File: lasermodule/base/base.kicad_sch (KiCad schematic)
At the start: 18 parts, among them J10 Conn_01x01, J11 Conn_01x01, J12 Conn_01x01, J19 2-1734248-0, J2 Conn_01x13, J6 mirrormotor, J7 Conn_01x01, J8 Conn_01x01, J9 Conn_01x01

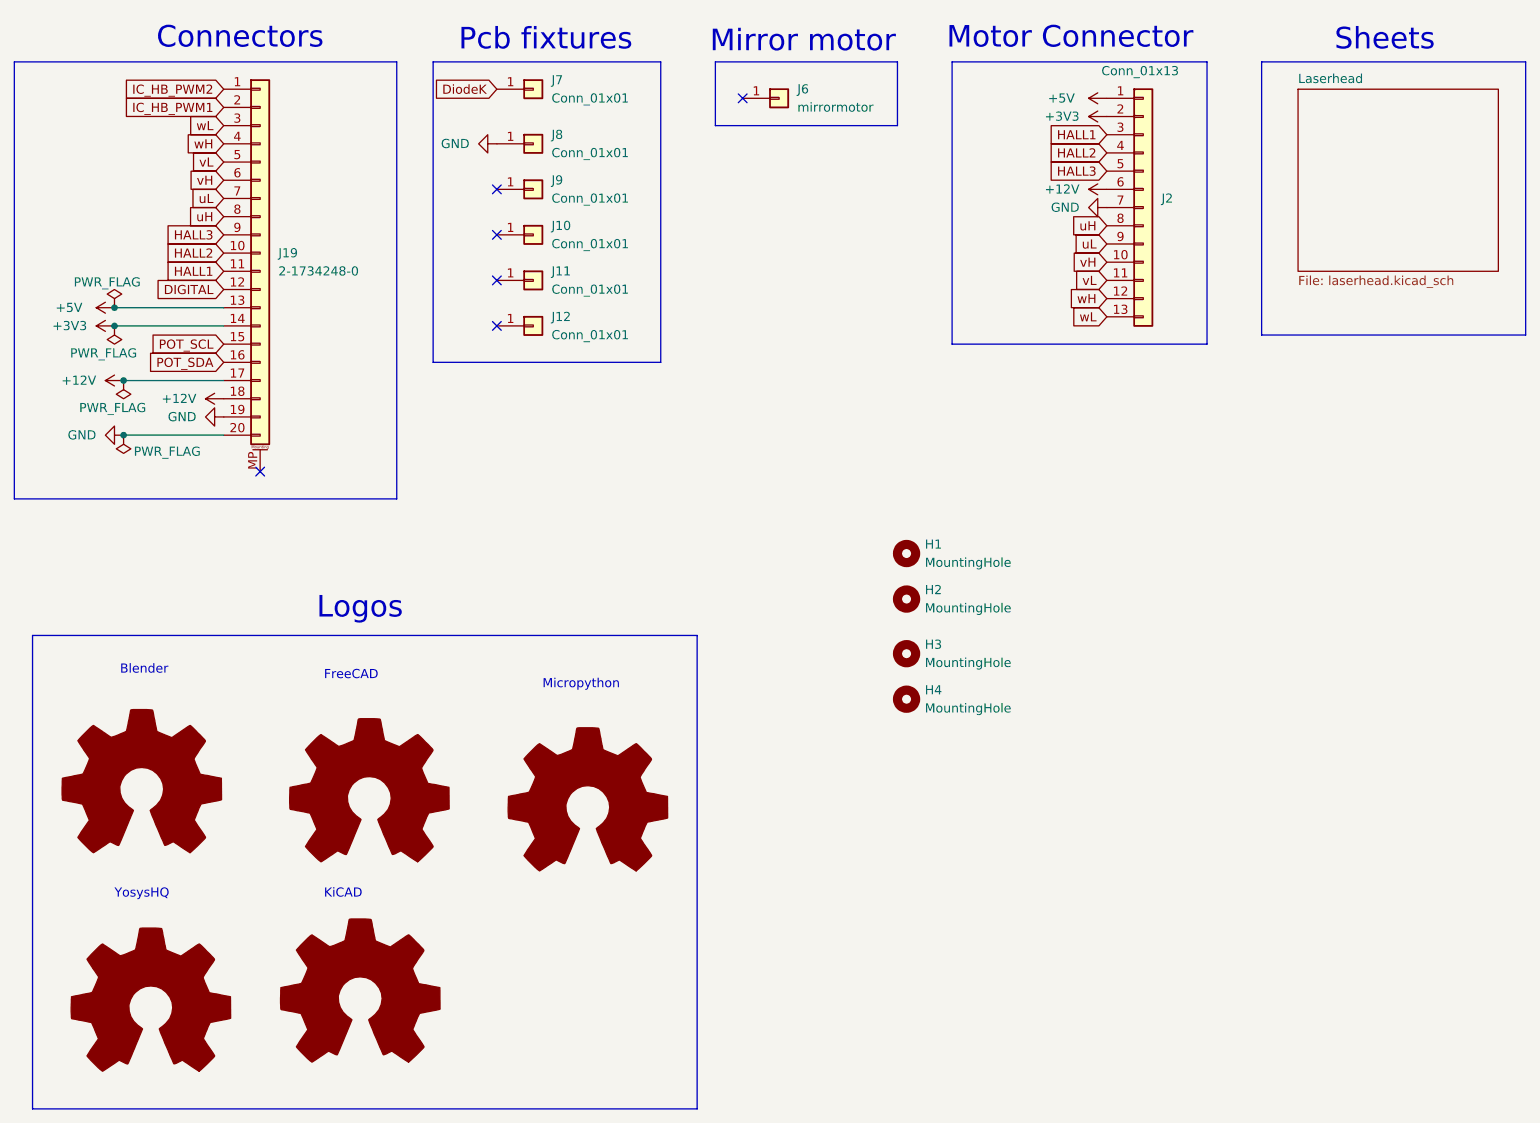
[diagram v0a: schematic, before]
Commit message: added mount felixprinter, standoffs
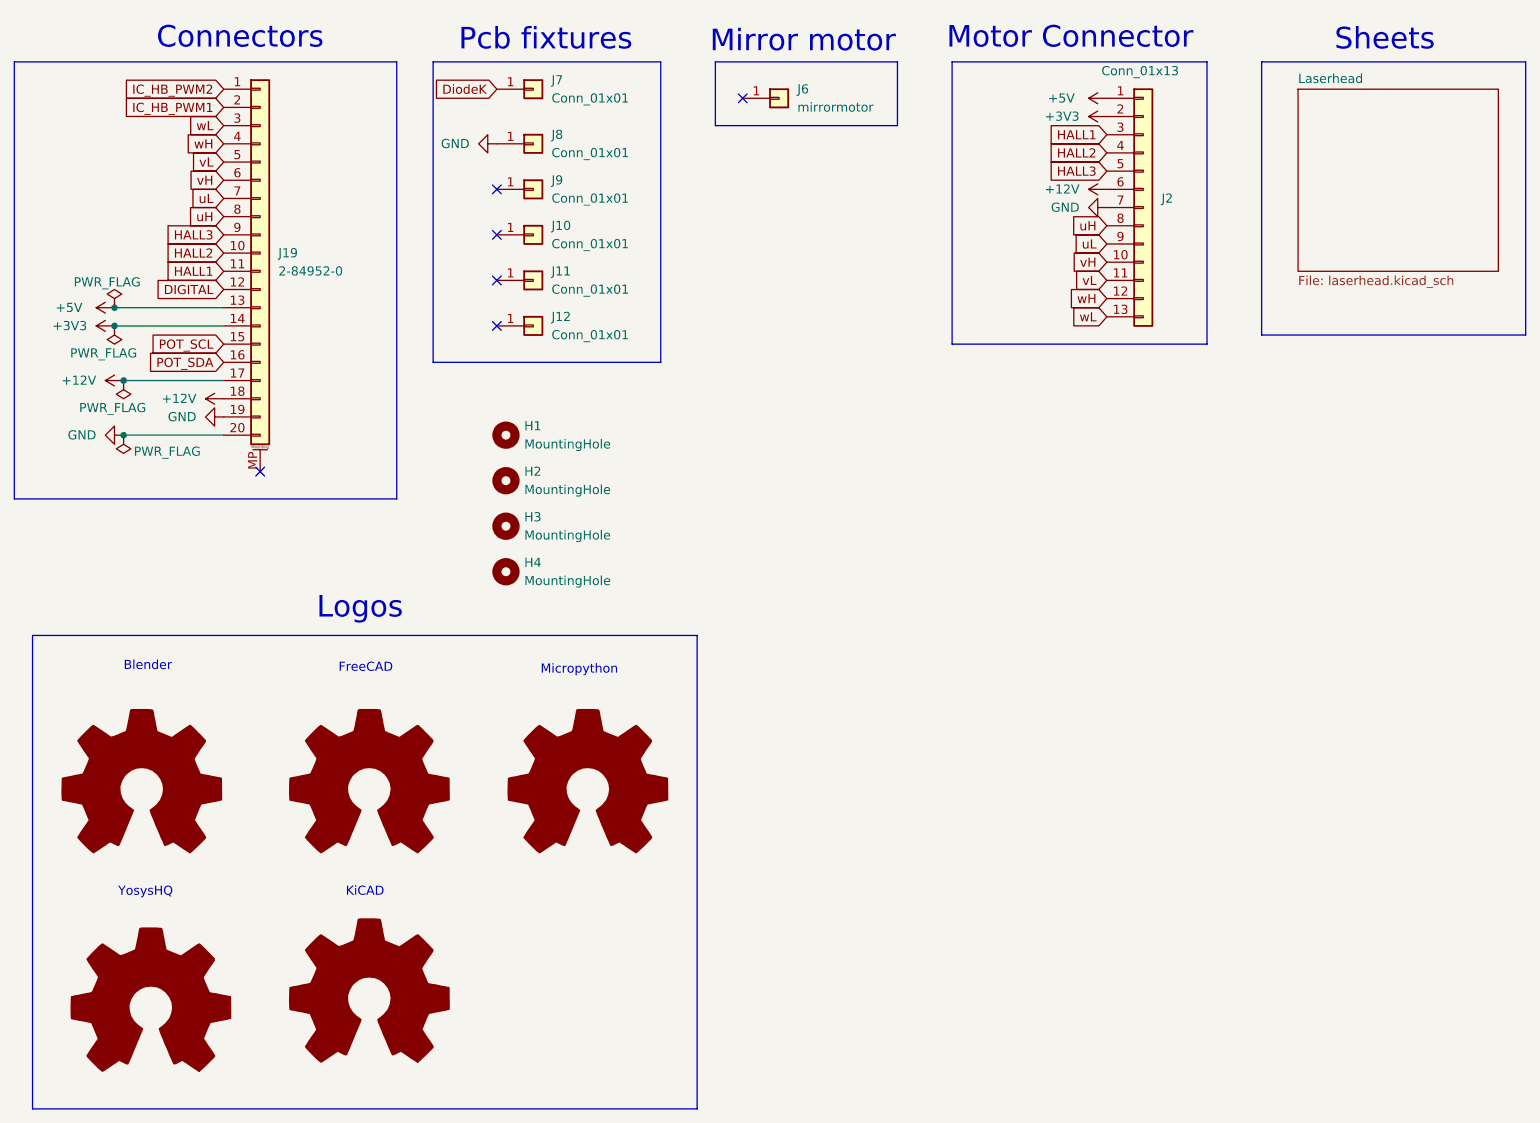
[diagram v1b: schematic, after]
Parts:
- H1, H2, H3, H4: manf# (none) -> 970050244; mouser# (none) -> 710-970050244
- J19: value 2-1734248-0 -> 2-84952-0
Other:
- moved on the sheet: H1, H2, H3, H4
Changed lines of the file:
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@@
 	(text "Micropython"
 		(exclude_from_sim no)
-		(at 101.6 129.54 0)
+		(at 101.346 127.508 0)
 		(effects
 			(font
@@
 	(text "YosysHQ"
 		(exclude_from_sim no)
-		(at 41.91 158.75 0)
+		(at 42.418 158.496 0)
 		(effects
 			(font
@@
 	(text "FreeCAD"
 		(exclude_from_sim no)
-		(at 71.12 128.27 0)
+		(at 73.152 127.254 0)
 		(effects
 			(font
@@
 	(text "KiCAD"
 		(exclude_from_sim no)
-		(at 71.12 158.75 0)
+		(at 74.168 158.496 0)
 		(effects
 			(font
@@
 	(text "Blender"
 		(exclude_from_sim no)
-		(at 42.672 127.508 0)
+		(at 43.18 127 0)
 		(effects
 			(font
@@
 	(symbol
 		(lib_id "Graphic:Logo_Open_Hardware_Large")
-		(at 76.2 172.72 0)
+		(at 77.47 172.72 0)
 		(unit 1)
 		(exclude_from_sim no)
@@
 		(dnp no)
 		(property "Reference" "L3"
-			(at 76.2 160.02 0)
+			(at 77.47 160.02 0)
 			(effects
 				(font
@@
 		)
 		(property "Value" "Logo_Open_Hardware_Large"
-			(at 76.2 182.88 0)
+			(at 77.47 182.88 0)
 			(effects
 				(font
@@
 		)
 		(property "Footprint" "sockets_scanhead:kicad"
-			(at 76.2 172.72 0)
+			(at 77.47 172.72 0)
 			(effects
 				(font
@@
 		)
 		(property "Datasheet" "~"
-			(at 76.2 172.72 0)
+			(at 77.47 172.72 0)
 			(effects
 				(font
@@
 		)
 		(property "Description" ""
-			(at 76.2 172.72 0)
+			(at 77.47 172.72 0)
 			(effects
 				(font
@@
 	(symbol
 		(lib_id "Mechanical:MountingHole")
-		(at 152.4 130.81 0)
+		(at 96.52 113.03 0)
 		(unit 1)
 		(exclude_from_sim yes)
@@
 		(fields_autoplaced yes)
 		(property "Reference" "H4"
-			(at 154.94 129.5399 0)
+			(at 99.06 111.7599 0)
 			(effects
 				(font
@@
 		)
 		(property "Value" "MountingHole"
-			(at 154.94 132.0799 0)
+			(at 99.06 114.2999 0)
 			(effects
 				(font
@@
 		)
 		(property "Footprint" "MountingHole:MountingHole_2.2mm_M2"
-			(at 152.4 130.81 0)
+			(at 96.52 113.03 0)
 			(effects
 				(font
@@
 		)
 		(property "Datasheet" "~"
-			(at 152.4 130.81 0)
+			(at 96.52 113.03 0)
 			(effects
 				(font
@@
 		)
 		(property "Description" "Mounting Hole without connection"
-			(at 152.4 130.81 0)
+			(at 96.52 113.03 0)
+			(effects
+				(font
+					(size 1.27 1.27)
+				)
+				(hide yes)
+			)
+		)
+		(property "manf#" "970050244"
+			(at 96.52 113.03 0)
+			(effects
+				(font
+					(size 1.27 1.27)
+				)
+				(hide yes)
+			)
+		)
+		(property "mouser#" "710-970050244"
+			(at 96.52 113.03 0)
 			(effects
 				(font
@@
 			)
 		)
-		(property "Value" "2-1734248-0"
+		(property "Value" "2-84952-0"
 			(at 64.77 71.1199 0)
 			(effects
@@
 	(symbol
 		(lib_id "Graphic:Logo_Open_Hardware_Large")
-		(at 107.95 146.05 0)
+		(at 107.95 143.51 0)
 		(unit 1)
 		(exclude_from_sim no)
@@
 		(dnp no)
 		(property "Reference" "L5"
-			(at 107.95 133.35 0)
+			(at 107.95 130.81 0)
 			(effects
 				(font
@@
 		)
 		(property "Value" "Logo_Open_Hardware_Large"
-			(at 107.95 156.21 0)
+			(at 107.95 153.67 0)
 			(effects
 				(font
@@
 		)
 		(property "Footprint" "sockets_scanhead:micropython"
-			(at 107.95 146.05 0)
+			(at 107.95 143.51 0)
 			(effects
 				(font
@@
 		)
 		(property "Datasheet" "~"
-			(at 107.95 146.05 0)
+			(at 107.95 143.51 0)
 			(effects
 				(font
@@
 		)
 		(property "Description" ""
-			(at 107.95 146.05 0)
+			(at 107.95 143.51 0)
 			(effects
 				(font
@@
 	(symbol
 		(lib_id "Mechanical:MountingHole")
-		(at 152.4 124.46 0)
+		(at 96.52 106.68 0)
 		(unit 1)
 		(exclude_from_sim yes)
@@
 		(fields_autoplaced yes)
 		(property "Reference" "H3"
-			(at 154.94 123.1899 0)
+			(at 99.06 105.4099 0)
 			(effects
 				(font
@@
 		)
 		(property "Value" "MountingHole"
-			(at 154.94 125.7299 0)
+			(at 99.06 107.9499 0)
 			(effects
 				(font
@@
 		)
 		(property "Footprint" "MountingHole:MountingHole_2.2mm_M2"
-			(at 152.4 124.46 0)
+			(at 96.52 106.68 0)
 			(effects
 				(font
@@
 		)
 		(property "Datasheet" "~"
-			(at 152.4 124.46 0)
+			(at 96.52 106.68 0)
 			(effects
 				(font
@@
 		)
 		(property "Description" "Mounting Hole without connection"
-			(at 152.4 124.46 0)
+			(at 96.52 106.68 0)
+			(effects
+				(font
+					(size 1.27 1.27)
+				)
+				(hide yes)
+			)
+		)
+		(property "manf#" "970050244"
+			(at 96.52 106.68 0)
+			(effects
+				(font
+					(size 1.27 1.27)
+				)
+				(hide yes)
+			)
+		)
+		(property "mouser#" "710-970050244"
+			(at 96.52 106.68 0)
 			(effects
 				(font
@@
 	(symbol
 		(lib_id "Mechanical:MountingHole")
-		(at 152.4 110.49 0)
+		(at 96.52 93.98 0)
 		(unit 1)
 		(exclude_from_sim yes)
@@
 		(fields_autoplaced yes)
 		(property "Reference" "H1"
-			(at 154.94 109.2199 0)
+			(at 99.06 92.7099 0)
 			(effects
 				(font
@@
 		)
 		(property "Value" "MountingHole"
-			(at 154.94 111.7599 0)
+			(at 99.06 95.2499 0)
 			(effects
 				(font
@@
 		)
 		(property "Footprint" "MountingHole:MountingHole_2.2mm_M2"
-			(at 152.4 110.49 0)
+			(at 96.52 93.98 0)
 			(effects
 				(font
@@
 		)
 		(property "Datasheet" "~"
-			(at 152.4 110.49 0)
+			(at 96.52 93.98 0)
 			(effects
 				(font
@@
 		)
 		(property "Description" "Mounting Hole without connection"
-			(at 152.4 110.49 0)
+			(at 96.52 93.98 0)
+			(effects
+				(font
+					(size 1.27 1.27)
+				)
+				(hide yes)
+			)
+		)
+		(property "mouser#" "710-970050244"
+			(at 96.52 93.98 0)
+			(effects
+				(font
+					(size 1.27 1.27)
+				)
+				(hide yes)
+			)
+		)
+		(property "manf#" "970050244"
+			(at 96.52 93.98 0)
 			(effects
 				(font
@@
 	(symbol
 		(lib_id "Mechanical:MountingHole")
-		(at 152.4 116.84 0)
+		(at 96.52 100.33 0)
 		(unit 1)
 		(exclude_from_sim yes)
@@
 		(fields_autoplaced yes)
 		(property "Reference" "H2"
-			(at 154.94 115.5699 0)
+			(at 99.06 99.0599 0)
 			(effects
 				(font
@@
 		)
 		(property "Value" "MountingHole"
-			(at 154.94 118.1099 0)
+			(at 99.06 101.5999 0)
 			(effects
 				(font
@@
 		)
 		(property "Footprint" "MountingHole:MountingHole_2.2mm_M2"
-			(at 152.4 116.84 0)
+			(at 96.52 100.33 0)
 			(effects
 				(font
@@
 		)
 		(property "Datasheet" "~"
-			(at 152.4 116.84 0)
+			(at 96.52 100.33 0)
 			(effects
 				(font
@@
 		)
 		(property "Description" "Mounting Hole without connection"
-			(at 152.4 116.84 0)
+			(at 96.52 100.33 0)
+			(effects
+				(font
+					(size 1.27 1.27)
+				)
+				(hide yes)
+			)
+		)
+		(property "manf#" "970050244"
+			(at 96.52 100.33 0)
+			(effects
+				(font
+					(size 1.27 1.27)
+				)
+				(hide yes)
+			)
+		)
+		(property "mouser#" "710-970050244"
+			(at 96.52 100.33 0)
 			(effects
 				(font
@@
 	(symbol
 		(lib_id "Graphic:Logo_Open_Hardware_Large")
-		(at 77.47 144.78 0)
+		(at 77.47 143.51 0)
 		(unit 1)
 		(exclude_from_sim no)
@@
 		(dnp no)
 		(property "Reference" "L4"
-			(at 77.47 132.08 0)
+			(at 77.47 130.81 0)
 			(effects
 				(font
@@
 		)
 		(property "Value" "Logo_Open_Hardware_Large"
-			(at 77.47 154.94 0)
+			(at 77.47 153.67 0)
 			(effects
 				(font
@@
 		)
 		(property "Footprint" "sockets_scanhead:freecad"
-			(at 77.47 144.78 0)
+			(at 77.47 143.51 0)
 			(effects
 				(font
@@
 		)
 		(property "Datasheet" "~"
-			(at 77.47 144.78 0)
+			(at 77.47 143.51 0)
 			(effects
 				(font
@@
 		)
 		(property "Description" ""
-			(at 77.47 144.78 0)
-			(effects
-				(font
+			(at 77.47 143.51 0)
+			(effects
+				(font

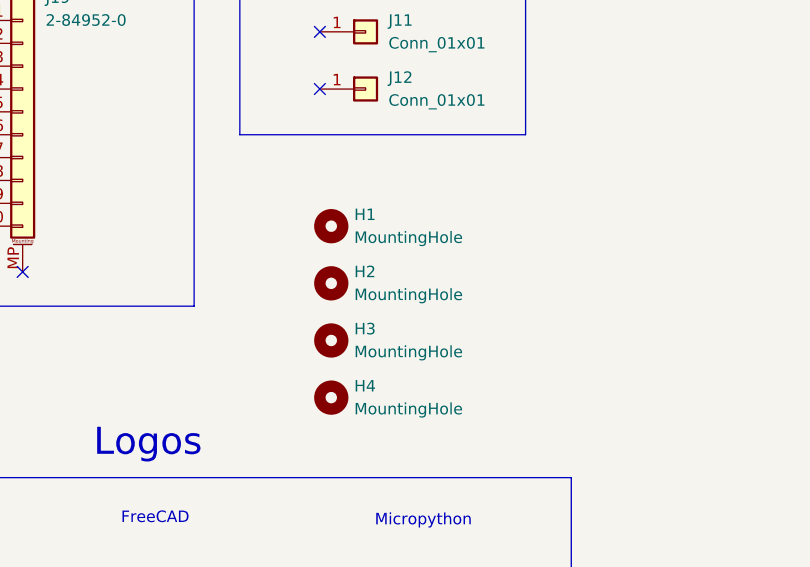
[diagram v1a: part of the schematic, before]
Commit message: changes to reduce prices pcbway
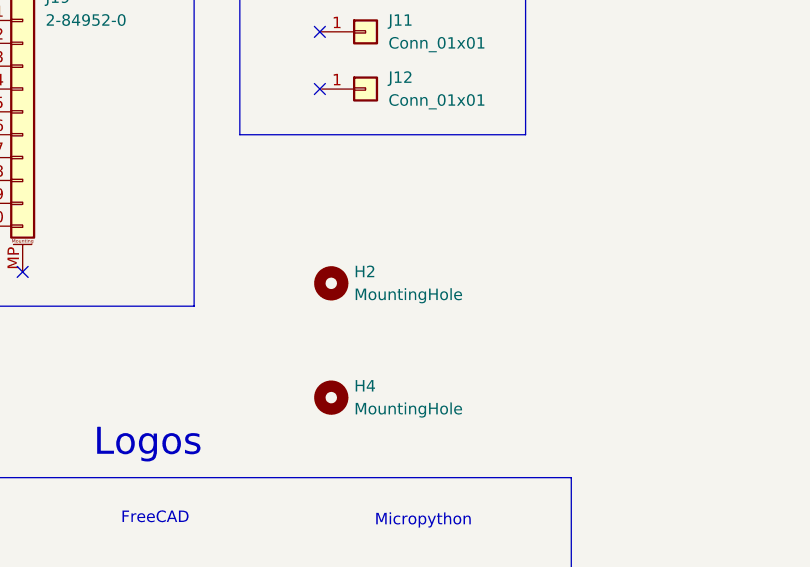
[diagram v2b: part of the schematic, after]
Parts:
- removed H1, H3: MountingHole, MountingHole:MountingHole_2.2mm_M2, symbol Mechanical:MountingHole
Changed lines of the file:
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@@
-	)
-	(symbol
-		(lib_id "Mechanical:MountingHole")
-		(at 96.52 106.68 0)
-		(unit 1)
-		(exclude_from_sim yes)
-		(in_bom no)
-		(on_board yes)
-		(dnp no)
-		(fields_autoplaced yes)
-		(property "Reference" "H3"
-			(at 99.06 105.4099 0)
-			(effects
-				(font
-					(size 1.27 1.27)
-				)
-				(justify left)
-			)
-		)
-		(property "Value" "MountingHole"
-			(at 99.06 107.9499 0)
-			(effects
-				(font
-					(size 1.27 1.27)
-				)
-				(justify left)
-			)
-		)
-		(property "Footprint" "MountingHole:MountingHole_2.2mm_M2"
-			(at 96.52 106.68 0)
-			(effects
-				(font
-					(size 1.27 1.27)
-				)
-				(hide yes)
-			)
-		)
-		(property "Datasheet" "~"
-			(at 96.52 106.68 0)
-			(effects
-				(font
-					(size 1.27 1.27)
-				)
-				(hide yes)
-			)
-		)
-		(property "Description" "Mounting Hole without connection"
-			(at 96.52 106.68 0)
-			(effects
-				(font
-					(size 1.27 1.27)
-				)
-				(hide yes)
-			)
-		)
-		(property "manf#" "970050244"
-			(at 96.52 106.68 0)
-			(effects
-				(font
-					(size 1.27 1.27)
-				)
-				(hide yes)
-			)
-		)
-		(property "mouser#" "710-970050244"
-			(at 96.52 106.68 0)
-			(effects
-				(font
-					(size 1.27 1.27)
-				)
-				(hide yes)
-			)
-		)
-		(instances
-			(project "base"
-				(path "/e63e39d7-6ac0-4ffd-8aa3-1841a4541b55"
-					(reference "H3")
-					(unit 1)
-				)
-			)
-		)
 	)
 	(symbol
@@
 					(unit 1)
 				)
-			)
-		)
-	)
-	(symbol
-		(lib_id "Mechanical:MountingHole")
-		(at 96.52 93.98 0)
-		(unit 1)
-		(exclude_from_sim yes)
-		(in_bom no)
-		(on_board yes)
-		(dnp no)
-		(fields_autoplaced yes)
-		(property "Reference" "H1"
-			(at 99.06 92.7099 0)
-			(effects
-				(font
-					(size 1.27 1.27)
-				)
-				(justify left)
-			)
-		)
-		(property "Value" "MountingHole"
-			(at 99.06 95.2499 0)
-			(effects
-				(font
-					(size 1.27 1.27)
-				)
-				(justify left)
-			)
-		)
-		(property "Footprint" "MountingHole:MountingHole_2.2mm_M2"
-			(at 96.52 93.98 0)
-			(effects
-				(font
-					(size 1.27 1.27)
-				)
-				(hide yes)
-			)
-		)
-		(property "Datasheet" "~"
-			(at 96.52 93.98 0)
-			(effects
-				(font
-					(size 1.27 1.27)
-				)
-				(hide yes)
-			)
-		)
-		(property "Description" "Mounting Hole without connection"
-			(at 96.52 93.98 0)
-			(effects
-				(font
-					(size 1.27 1.27)
-				)
-				(hide yes)
-			)
-		)
-		(property "mouser#" "710-970050244"
-			(at 96.52 93.98 0)
-			(effects
-				(font
-					(size 1.27 1.27)
-				)
-				(hide yes)
-			)
-		)
-		(property "manf#" "970050244"
-			(at 96.52 93.98 0)
-			(effects
-				(font
-					(size 1.27 1.27)
-				)
-				(hide yes)
-			)
-		)
-		(instances
-			(project "base"
-				(path "/e63e39d7-6ac0-4ffd-8aa3-1841a4541b55"
-					(reference "H1")
-					(unit 1)
-				)

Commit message: sent to pcbway
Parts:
- added H1, H3: MountingHole, MountingHole:MountingHole_2.2mm_M2, symbol Mechanical:MountingHole
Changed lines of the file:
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@@
+	)
+	(symbol
+		(lib_id "Mechanical:MountingHole")
+		(at 96.52 93.98 0)
+		(unit 1)
+		(exclude_from_sim yes)
+		(in_bom no)
+		(on_board yes)
+		(dnp no)
+		(fields_autoplaced yes)
+		(property "Reference" "H1"
+			(at 99.06 92.7099 0)
+			(effects
+				(font
+					(size 1.27 1.27)
+				)
+				(justify left)
+			)
+		)
+		(property "Value" "MountingHole"
+			(at 99.06 95.2499 0)
+			(effects
+				(font
+					(size 1.27 1.27)
+				)
+				(justify left)
+			)
+		)
+		(property "Footprint" "MountingHole:MountingHole_2.2mm_M2"
+			(at 96.52 93.98 0)
+			(effects
+				(font
+					(size 1.27 1.27)
+				)
+				(hide yes)
+			)
+		)
+		(property "Datasheet" "~"
+			(at 96.52 93.98 0)
+			(effects
+				(font
+					(size 1.27 1.27)
+				)
+				(hide yes)
+			)
+		)
+		(property "Description" "Mounting Hole without connection"
+			(at 96.52 93.98 0)
+			(effects
+				(font
+					(size 1.27 1.27)
+				)
+				(hide yes)
+			)
+		)
+		(property "manf#" "970050244"
+			(at 96.52 93.98 0)
+			(effects
+				(font
+					(size 1.27 1.27)
+				)
+				(hide yes)
+			)
+		)
+		(property "mouser#" "710-970050244"
+			(at 96.52 93.98 0)
+			(effects
+				(font
+					(size 1.27 1.27)
+				)
+				(hide yes)
+			)
+		)
+		(instances
+			(project "base"
+				(path "/e63e39d7-6ac0-4ffd-8aa3-1841a4541b55"
+					(reference "H1")
+					(unit 1)
+				)
+			)
+		)
 	)
 	(symbol
@@
 					(unit 1)
 				)
+			)
+		)
+	)
+	(symbol
+		(lib_id "Mechanical:MountingHole")
+		(at 96.52 106.68 0)
+		(unit 1)
+		(exclude_from_sim yes)
+		(in_bom no)
+		(on_board yes)
+		(dnp no)
+		(fields_autoplaced yes)
+		(property "Reference" "H3"
+			(at 99.06 105.4099 0)
+			(effects
+				(font
+					(size 1.27 1.27)
+				)
+				(justify left)
+			)
+		)
+		(property "Value" "MountingHole"
+			(at 99.06 107.9499 0)
+			(effects
+				(font
+					(size 1.27 1.27)
+				)
+				(justify left)
+			)
+		)
+		(property "Footprint" "MountingHole:MountingHole_2.2mm_M2"
+			(at 96.52 106.68 0)
+			(effects
+				(font
+					(size 1.27 1.27)
+				)
+				(hide yes)
+			)
+		)
+		(property "Datasheet" "~"
+			(at 96.52 106.68 0)
+			(effects
+				(font
+					(size 1.27 1.27)
+				)
+				(hide yes)
+			)
+		)
+		(property "Description" "Mounting Hole without connection"
+			(at 96.52 106.68 0)
+			(effects
+				(font
+					(size 1.27 1.27)
+				)
+				(hide yes)
+			)
+		)
+		(property "manf#" "970050244"
+			(at 96.52 106.68 0)
+			(effects
+				(font
+					(size 1.27 1.27)
+				)
+				(hide yes)
+			)
+		)
+		(property "mouser#" "710-970050244"
+			(at 96.52 106.68 0)
+			(effects
+				(font
+					(size 1.27 1.27)
+				)
+				(hide yes)
+			)
+		)
+		(instances
+			(project "base"
+				(path "/e63e39d7-6ac0-4ffd-8aa3-1841a4541b55"
+					(reference "H3")
+					(unit 1)
+				)
